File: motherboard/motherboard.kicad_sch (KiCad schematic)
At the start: 54 parts, among them J1 Raspberry_Pi_2_3 ANT, J14 USB_C_Receptacle_USB2.0, J2 PROGRAM, J3 Battery / Pitot/ Orientation, J4 c02 censor, J5 shaftencorder, J7 SparLoad, J8 lidar, J9 Control Board, Q1 2N7002K, SW1 MCU_RST, U1 Bluetooth Module - Shaft Power, U2 IMU, U3 Bluetooth Module - Power Cont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, U4 GPS module, U5 DHT11(DHT22), U6 STM32F412RETx, U7 nRF24L01-telemetry-INTERIOR, U8 nRF24L01-telemetry-EXTERIOR, U9 DPS310 - barometer, Y1 8M

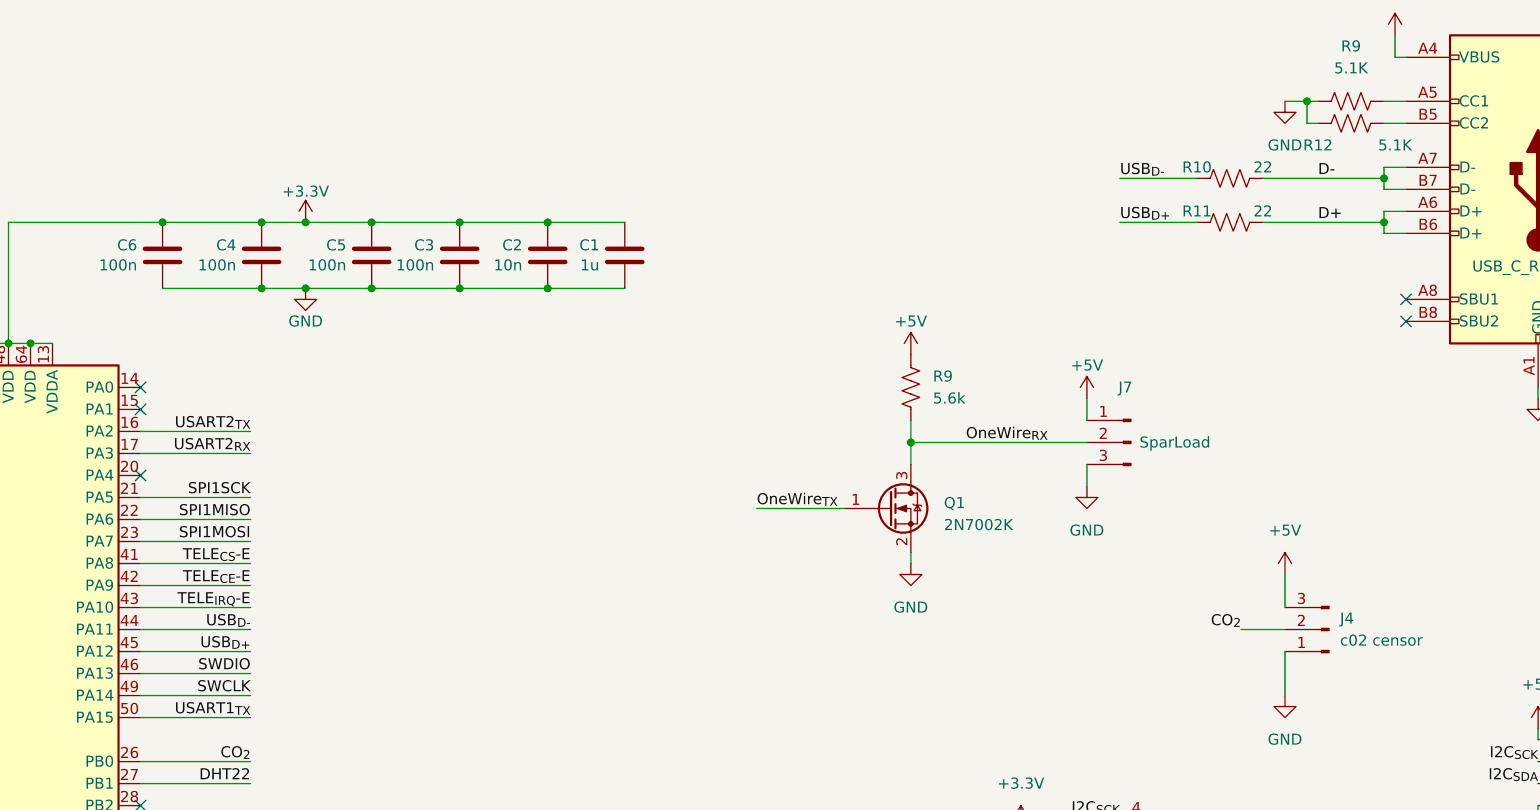
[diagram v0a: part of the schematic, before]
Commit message: PCB Rev2 Layout
PCB layout revised with ground and power pours, differential routing for USB, fixes for USB and programming pins. Passes DRC.
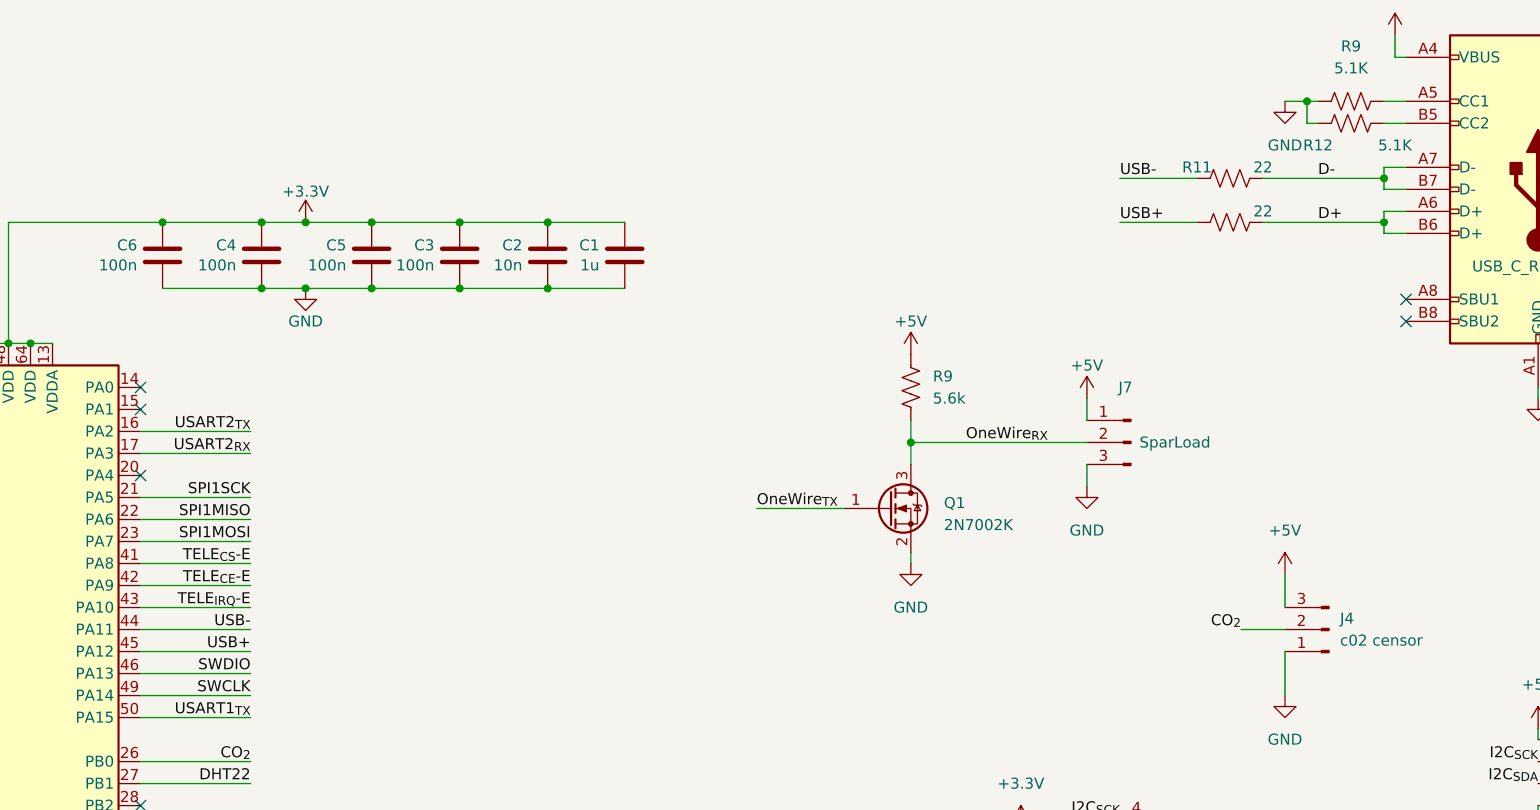
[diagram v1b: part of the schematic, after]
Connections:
- net D+: now also R10.2; no longer R11.2
- net D-: now also R11.2; no longer R10.2
- net USB_{D+} renamed USB+
- net USB+: now also R10.1; no longer R11.1
- net USB_{D-} renamed USB-
- net USB-: now also R11.1; no longer R10.1
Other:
- moved on the sheet: R11
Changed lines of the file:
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@@
   (junction (at 271.78 58.42) (diameter 0) (color 0 0 0 0)
   )
-  (junction (at 378.46 45.72) (diameter 0) (color 0 0 0 0)
-  )
   (junction (at 369.57 207.01) (diameter 0) (color 0 0 0 0)
   )
@@
   (junction (at 219.71 64.77) (diameter 0) (color 0 0 0 0)
   )
-  (junction (at 378.46 50.8) (diameter 0) (color 0 0 0 0)
-  )
   (junction (at 60.96 99.06) (diameter 0) (color 0 0 0 0)
   )
@@
   (junction (at 54.61 199.39) (diameter 0) (color 0 0 0 0)
   )
+  (junction (at 378.46 50.8) (diameter 0) (color 0 0 0 0)
+  )
   (junction (at 237.49 50.8) (diameter 0) (color 0 0 0 0)
   )
@@
   (junction (at 219.71 156.21) (diameter 0) (color 0 0 0 0)
   )
+  (junction (at 378.46 45.72) (diameter 0) (color 0 0 0 0)
+  )
   (no_connect (at 234.95 118.11))
   (no_connect (at 38.1 83.82))
@@
     (stroke (width 0) (type default))
   )
+  (wire (pts (xy 364.49 45.72) (xy 378.46 45.72))
+    (stroke (width 0) (type default))
+  )
   (wire (pts (xy 176.53 240.03) (xy 176.53 250.19))
     (stroke (width 0) (type default))
@@
     (stroke (width 0) (type default))
   )
-  (wire (pts (xy 378.46 50.8) (xy 364.49 50.8))
-    (stroke (width 0) (type default))
-  )
   (wire (pts (xy 369.57 36.83) (xy 370.84 36.83))
     (stroke (width 0) (type default))
@@
     (stroke (width 0) (type default))
   )
+  (wire (pts (xy 347.98 50.8) (xy 356.87 50.8))
+    (stroke (width 0) (type default))
+  )
   (wire (pts (xy 234.95 107.95) (xy 247.65 107.95))
     (stroke (width 0) (type default))
   )
+  (wire (pts (xy 378.46 50.8) (xy 378.46 52.07))
+    (stroke (width 0) (type default))
+  )
   (wire (pts (xy 328.93 166.37) (xy 340.36 166.37))
     (stroke (width 0) (type default))
@@
     (stroke (width 0) (type default))
   )
+  (wire (pts (xy 378.46 45.72) (xy 378.46 46.99))
+    (stroke (width 0) (type default))
+  )
   (wire (pts (xy 248.92 50.8) (xy 254 50.8))
     (stroke (width 0) (type default))
@@
     (stroke (width 0) (type default))
   )
-  (wire (pts (xy 378.46 45.72) (xy 378.46 44.45))
+  (wire (pts (xy 378.46 44.45) (xy 378.46 45.72))
     (stroke (width 0) (type default))
   )
@@
     (stroke (width 0) (type default))
   )
-  (wire (pts (xy 378.46 46.99) (xy 378.46 45.72))
-    (stroke (width 0) (type default))
-  )
   (wire (pts (xy 248.92 58.42) (xy 254 58.42))
     (stroke (width 0) (type default))
@@
     (stroke (width 0) (type default))
   )
-  (wire (pts (xy 378.46 50.8) (xy 378.46 52.07))
-    (stroke (width 0) (type default))
-  )
   (wire (pts (xy 247.65 138.43) (xy 234.95 138.43))
     (stroke (width 0) (type default))
@@
     (stroke (width 0) (type default))
   )
-  (wire (pts (xy 347.98 45.72) (xy 356.87 45.72))
-    (stroke (width 0) (type default))
-  )
-  (wire (pts (xy 364.49 45.72) (xy 378.46 45.72))
+  (wire (pts (xy 234.95 120.65) (xy 247.65 120.65))
     (stroke (width 0) (type default))
   )
-  (wire (pts (xy 234.95 120.65) (xy 247.65 120.65))
+  (wire (pts (xy 364.49 50.8) (xy 378.46 50.8))
     (stroke (width 0) (type default))
   )
@@
     (stroke (width 0) (type default))
   )
+  (wire (pts (xy 347.98 45.72) (xy 356.87 45.72))
+    (stroke (width 0) (type default))
+  )
   (wire (pts (xy 234.95 146.05) (xy 247.65 146.05))
     (stroke (width 0) (type default))
@@
     (stroke (width 0) (type default))
   )
-  (wire (pts (xy 347.98 50.8) (xy 356.87 50.8))
-    (stroke (width 0) (type default))
-  )
   (wire (pts (xy 396.24 151.13) (xy 394.97 151.13))
     (stroke (width 0) (type default))
@@
     (effects (font (size 1.27 1.27)) (justify right bottom))
   )
-  (label "USB_{D+}" (at 247.65 100.33 180) (fields_autoplaced)
+  (label "USB+" (at 247.65 100.33 180) (fields_autoplaced)
     (effects (font (size 1.27 1.27)) (justify right bottom))
   )
@@
     (effects (font (size 1.27 1.27)) (justify right bottom))
   )
-  (label "USB_{D-}" (at 247.65 97.79 180) (fields_autoplaced)
+  (label "USB-" (at 247.65 97.79 180) (fields_autoplaced)
     (effects (font (size 1.27 1.27)) (justify right bottom))
   )
@@
     (effects (font (size 1.27 1.27)) (justify right bottom))
   )
-  (label "USB_{D+}" (at 347.98 50.8 0) (fields_autoplaced)
+  (label "USB+" (at 347.98 50.8 0) (fields_autoplaced)
     (effects (font (size 1.27 1.27)) (justify left bottom))
   )
@@
     (effects (font (size 1.27 1.27)) (justify right bottom))
   )
-  (label "USB_{D-}" (at 347.98 45.72 0) (fields_autoplaced)
+  (label "USB-" (at 347.98 45.72 0) (fields_autoplaced)
     (effects (font (size 1.27 1.27)) (justify left bottom))
   )
@@
     )
   )
-  (symbol (lib_id "Device:R_US") (at 360.68 45.72 90) (unit 1)
+  (symbol (lib_id "Device:R_US") (at 360.68 50.8 90) (unit 1)
     (in_bom yes) (on_board yes) (dnp no)
-    (property "Reference" "R10" (at 356.87 44.45 90)
-      (effects (font (size 1.27 1.27)))
+    (property "Reference" "R10" (at 356.87 49.53 90)
+      (effects (font (size 1.27 1.27)) hide)
     )
-    (property "Value" "22" (at 364.49 44.45 90)
+    (property "Value" "22" (at 364.49 49.53 90)
       (effects (font (size 1.27 1.27)))
     )
-    (property "Footprint" "Resistor_SMD:R_0603_1608Metric" (at 360.934 44.704 90)
+    (property "Footprint" "Resistor_SMD:R_0603_1608Metric" (at 360.934 49.784 90)
       (effects (font (size 1.27 1.27)) hide)
     )
-    (property "Datasheet" "~" (at 360.68 45.72 0)
+    (property "Datasheet" "~" (at 360.68 50.8 0)
       (effects (font (size 1.27 1.27)) hide)
     )
@@
     )
   )
-  (symbol (lib_id "Device:R_US") (at 360.68 50.8 90) (unit 1)
+  (symbol (lib_id "Device:R_US") (at 360.68 45.72 90) (unit 1)
     (in_bom yes) (on_board yes) (dnp no)
-    (property "Reference" "R11" (at 356.87 49.53 90)
+    (property "Reference" "R11" (at 356.87 44.45 90)
       (effects (font (size 1.27 1.27)))
     )
-    (property "Value" "22" (at 364.49 49.53 90)
+    (property "Value" "22" (at 364.49 44.45 90)
       (effects (font (size 1.27 1.27)))
     )
-    (property "Footprint" "Resistor_SMD:R_0603_1608Metric" (at 360.934 49.784 90)
+    (property "Footprint" "Resistor_SMD:R_0603_1608Metric" (at 360.934 44.704 90)
       (effects (font (size 1.27 1.27)) hide)
     )
-    (property "Datasheet" "~" (at 360.68 50.8 0)
+    (property "Datasheet" "~" (at 360.68 45.72 0)
       (effects (font (size 1.27 1.27)) hide)
     )

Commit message: Motherboard Revision 3 Initial Commit
Motherboard updated with pull up resistors, decoupling capacitors, on board regulator, op-amp for magnetic encoder, and more.
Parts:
- removed J2: PROGRAM, Connector_PinSocket_2.54mm:PinSocket_1x04_P2.54mm_Vertical, symbol Connector:Conn_01x04_Pin
- removed U1: Bluetooth Module - Shaft Power, Connector_PinSocket_2.54mm:PinSocket_1x06_P2.54mm_Vertical, symbol mb_sensors:HC-05
- removed U3: Bluetooth Module - Power Controller, Connector_PinSocket_2.54mm:PinSocket_1x06_P2.54mm_Vertical, symbol mb_sensors:HC-05
- added C13, C17: 0.22u, Capacitor_SMD:C_0603_1608Metric, symbol Device:C
- added C15: 10n, Capacitor_SMD:C_0603_1608Metric, symbol Device:C
- added C16, C4: 100n, Capacitor_SMD:C_0603_1608Metric, symbol Device:C
- added C3: 2.2u, Capacitor_SMD:C_0603_1608Metric, symbol Device:C
- added J10: Programmer, Connector_PinHeader_1.27mm:PinHeader_2x07_P1.27mm_Vertical_SMD, symbol Connector_Generic:Conn_02x07_Odd_Even
- added JP2: opamp out, Jumper:SolderJumper-2_P1.3mm_Open_RoundedPad1.0x1.5mm, symbol Jumper:Jumper_2_Open
- added JP3: op-amp bypass, Jumper:SolderJumper-2_P1.3mm_Open_RoundedPad1.0x1.5mm, symbol Jumper:Jumper_2_Open
- added JP4: 5V, Jumper:SolderJumper-2_P1.3mm_Open_RoundedPad1.0x1.5mm, symbol Jumper:Jumper_2_Open
- added JP5, JP6: Jumper_2_Open, Jumper:SolderJumper-2_P1.3mm_Open_RoundedPad1.0x1.5mm, symbol Jumper:Jumper_2_Open
- added R13, R14: 10k, Resistor_SMD:R_0603_1608Metric, symbol Device:R
- added R15: 1k, Resistor_SMD:R_0603_1608Metric, symbol Device:R
- added R16: 20k, Resistor_SMD:R_0603_1608Metric, symbol Device:R
- added R17: 470R, Resistor_SMD:R_0603_1608Metric, symbol Device:R
- added U10: TLV76733DRVx, Package_SON:WSON-6-1EP_2x2mm_P0.65mm_EP1x1.6mm_ThermalVias, symbol Regulator_Linear:TLV76733DRVx
- added U3: LM358, Package_SO:SOIC-8-1EP_3.9x4.9mm_P1.27mm_EP2.29x3mm, symbol Amplifier_Operational:LM358
- J5: footprint Connector_JST:JST_EH_B3B-EH-A_1x03_P2.50mm_Vertical -> Connector_JST:JST_EH_B6B-EH-A_1x06_P2.50mm_Vertical; symbol Connector:Conn_01x03_Pin -> Connector:Conn_01x06_Pin
- R10, R11: value 22 -> 22R
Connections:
- net +3.3V: now also C3.1, C4.1, J10.3 (Pin_3), JP5.2 (B), R13.1, R14.1; no longer J5.3 (Pin_3)
- net +5V: now also J5.6 (Pin_6), C16.1, JP4.2 (B), JP6.1 (A), R16.1, U3.8 (V+)
- net GND: now also C13.2, C15.2, C16.2, C17.2, C3.2, C4.2, J10.5 (Pin_5), J10.7 (Pin_7), R15.2, U10.3 (GND), U10.5 (GND), U10.7 (PAD), U3.4 (V-)
- net I2C_{SCK}: now also R13.2
- net I2C_{SDA}: now also R14.2
- net SHAFTENC: now also C15.1, JP3.1 (A), R17.2, U3.3 (+); no longer U6.61 (PB8)
- net SWCLK: now also J10.6 (Pin_6)
- net SWDIO: now also J10.4 (Pin_4)
- net ENC2: now reaches U6.2 (PC13)
- net ENC2: now also J5.4 (Pin_4)
- net ENC3: now reaches U6.3 (PC14)
- net ENC3: now also J5.5 (Pin_5)
- net ENC1: now reaches U6.53 (PC12)
- net ENC1: now also J5.3 (Pin_3)
- new net: JP4.1 (A), R17.1
- new net: C13.1, JP5.1 (A), U10.1 (OUT), U10.2 (SNS)
- new net: JP2.1 (A), U3.1
- new net: R15.1, R16.2, U3.2 (-)
- new net: C17.1, JP6.2 (B), U10.4 (EN), U10.6 (IN)
- new net RPM: JP2.2 (B), JP3.2 (B), U6.61 (PB8)
- no-connect marks 57 -> 53
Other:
- moved on the sheet: C1, C11, C12, H1, H3, H4, H5, H6, H7, H8, J3, J4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

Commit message: Updated with Savo's suggested changes
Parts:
- removed J10: Programmer, Connector_PinHeader_1.27mm:PinHeader_2x07_P1.27mm_Vertical_SMD, symbol Connector_Generic:Conn_02x07_Odd_Even
- removed JP2: opamp out, Jumper:SolderJumper-2_P1.3mm_Open_RoundedPad1.0x1.5mm, symbol Jumper:Jumper_2_Open
- removed JP3: op-amp bypass, Jumper:SolderJumper-2_P1.3mm_Open_RoundedPad1.0x1.5mm, symbol Jumper:Jumper_2_Open
- removed R8: 10k, Resistor_SMD:R_0603_1608Metric, symbol Device:R_US
- added J2: Conn_ST_STDC14, Connector_PinHeader_1.27mm:PinHeader_2x07_P1.27mm_Vertical_SMD, symbol Connector:Conn_ST_STDC14
- JP1: value BOOT0 -> Jumper_3_Open; now in the parts list
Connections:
- net RPM is gone; now on net SHAFTENC OUT: U6.61 (PB8)
- net +3.3V: now also J2.3 (VCC); no longer JP1.3 (B)
- net GND: now also U6.60 (BOOT0), J2.11 (GNDDetect), J2.5 (GND), J2.7 (GND); no longer JP1.1 (A)
- net SWCLK: now also J2.6 (JCLK/SWCLK)
- net SWDIO: now also J2.4 (JTMS/SWDIO)
- net USART2_{RX}: now also J2.13 (VCP_RX)
- net USART2_{TX}: now also J2.14 (VCP_TX)
- net at U3.1: now also JP1.3 (B)
- net BOOT0 renamed SHAFTENC OUT
- net SHAFTENC OUT: no longer U6.60 (BOOT0)
- net SHAFTENC renamed SHAFTENC IN
- net SHAFTENC IN: now also JP1.1 (A)
- net USART6_{RX}: no longer names the net of U6.38 (PC7)
- net USART6_{TX}: no longer names the net of U6.37 (PC6)
- no-connect marks 53 -> 59

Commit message: Updated schematic symbols
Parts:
- J14: symbol Connector:USB_C_Receptacle_USB2.0 -> Connector:USB_C_Receptacle_USB2.0_16P
- R1, R10, R11, R12, R2, R3, R9: symbol Device:R_US -> Device:R
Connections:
- net at J1.1 (3V3): now also J1.17 (3V3)
- no-connect marks 59 -> 58

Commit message: Changed voltage regulator footprint
Removed thermal vias since they were too small for manufacturing.
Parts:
- U10: footprint Package_SON:WSON-6-1EP_2x2mm_P0.65mm_EP1x1.6mm_ThermalVias -> Package_SON:WSON-6-1EP_2x2mm_P0.65mm_EP1x1.6mm
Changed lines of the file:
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@@
 			)
 		)
-		(property "Footprint" "Package_SON:WSON-6-1EP_2x2mm_P0.65mm_EP1x1.6mm_ThermalVias"
+		(property "Footprint" "Package_SON:WSON-6-1EP_2x2mm_P0.65mm_EP1x1.6mm"
 			(at 276.86 190.5 0)
 			(effects
